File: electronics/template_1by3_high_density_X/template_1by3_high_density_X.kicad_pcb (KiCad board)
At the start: 2 copper layers, 19 x 26.5 mm, 10 parts, among them J1 1, J2 2, J3 3, J4 4, J5 5, J6 6, J7 7, J8 8

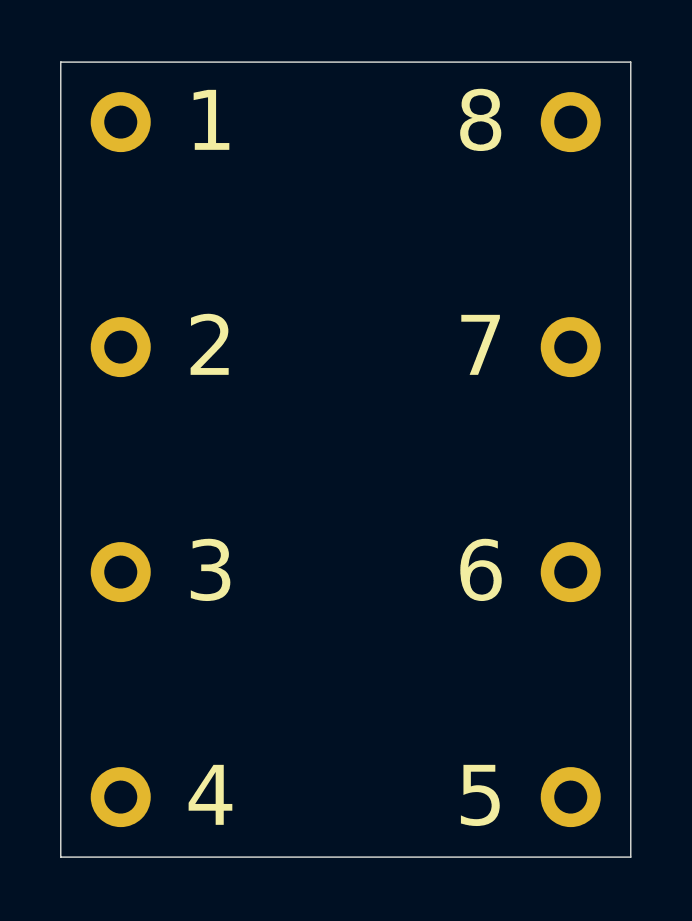
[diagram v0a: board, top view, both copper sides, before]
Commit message: completed high density X templates, updated versionnumbers of high density XN templates
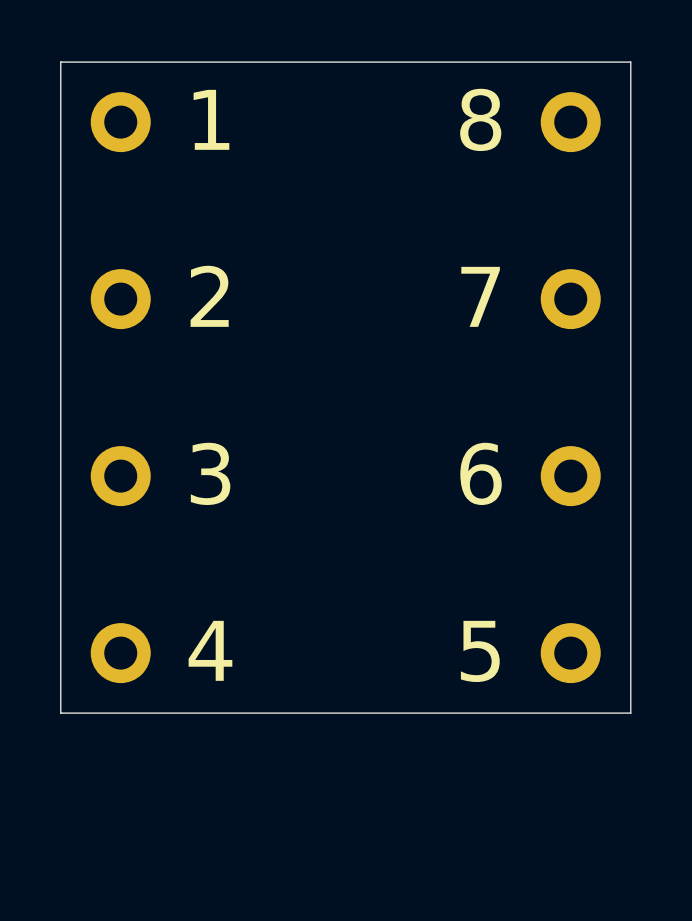
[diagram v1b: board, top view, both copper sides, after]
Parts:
- N1: value V20220113 -> V20240506
- moved J4 4.80 mm to (142.5, 80.2)
- moved J5 4.80 mm to (157.5, 80.2)
- moved J3 3.20 mm to (142.5, 74.3)
- moved J6 3.20 mm to (157.5, 74.3)
- moved N1 2.50 mm to (150.9, 74.7)
- moved N2 2.50 mm to (150.0, 71.0)
- moved J2 1.60 mm to (142.5, 68.4)
- moved J7 1.60 mm to (157.5, 68.4)
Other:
- board size 19 x 26.5 mm -> 19 x 21.7 mm
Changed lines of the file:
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@@
   (footprint "mill-max:PC_pin_nail_head_6092" locked (layer "F.Cu")
     (at 142.5 62.5)
-    (property "Sheetfile" "template_1by3.kicad_sch")
+    (property "Sheetfile" "template_1by3_high_density_X.kicad_sch")
     (property "Sheetname" "")
     (property "ki_description" "Generic connector, single row, 01x01, script generated (kicad-library-utils/schlib/autogen/connector/)")
@@
   )
   (footprint "mill-max:PC_pin_nail_head_6092" locked (layer "F.Cu")
-    (at 142.5 70)
-    (property "Sheetfile" "template_1by3.kicad_sch")
+    (at 142.5 68.4)
+    (property "Sheetfile" "template_1by3_high_density_X.kicad_sch")
     (property "Sheetname" "")
     (property "ki_description" "Generic connector, single row, 01x01, script generated (kicad-library-utils/schlib/autogen/connector/)")
@@
   )
   (footprint "mill-max:PC_pin_nail_head_6092" locked (layer "F.Cu")
-    (at 142.5 77.5)
-    (property "Sheetfile" "template_1by3.kicad_sch")
+    (at 142.5 74.3)
+    (property "Sheetfile" "template_1by3_high_density_X.kicad_sch")
     (property "Sheetname" "")
     (property "ki_description" "Generic connector, single row, 01x01, script generated (kicad-library-utils/schlib/autogen/connector/)")
@@
   )
   (footprint "mill-max:PC_pin_nail_head_6092" locked (layer "F.Cu")
-    (at 157.5 85)
-    (property "Sheetfile" "template_1by3.kicad_sch")
+    (at 157.5 80.2)
+    (property "Sheetfile" "template_1by3_high_density_X.kicad_sch")
     (property "Sheetname" "")
     (property "ki_description" "Generic connector, single row, 01x01, script generated (kicad-library-utils/schlib/autogen/connector/)")
@@
   )
   (footprint "mill-max:PC_pin_nail_head_6092" locked (layer "F.Cu")
-    (at 157.5 77.5)
-    (property "Sheetfile" "template_1by3.kicad_sch")
+    (at 157.5 74.3)
+    (property "Sheetfile" "template_1by3_high_density_X.kicad_sch")
     (property "Sheetname" "")
     (property "ki_description" "Generic connector, single row, 01x01, script generated (kicad-library-utils/schlib/autogen/connector/)")
@@
   )
   (footprint "mill-max:PC_pin_nail_head_6092" locked (layer "F.Cu")
-    (at 142.5 85 180)
-    (property "Sheetfile" "template_1by3.kicad_sch")
+    (at 142.5 80.2 180)
+    (property "Sheetfile" "template_1by3_high_density_X.kicad_sch")
     (property "Sheetname" "")
     (property "ki_description" "Generic connector, single row, 01x01, script generated (kicad-library-utils/schlib/autogen/connector/)")
@@
   (footprint "mill-max:PC_pin_nail_head_6092" locked (layer "F.Cu")
     (at 157.5 62.5)
-    (property "Sheetfile" "template_1by3.kicad_sch")
+    (property "Sheetfile" "template_1by3_high_density_X.kicad_sch")
     (property "Sheetname" "")
     (property "ki_description" "Generic connector, single row, 01x01, script generated (kicad-library-utils/schlib/autogen/connector/)")
@@
   )
   (footprint "mill-max:PC_pin_nail_head_6092" locked (layer "F.Cu")
-    (at 157.5 70)
-    (property "Sheetfile" "template_1by3.kicad_sch")
+    (at 157.5 68.4)
+    (property "Sheetfile" "template_1by3_high_density_X.kicad_sch")
     (property "Sheetname" "")
     (property "ki_description" "Generic connector, single row, 01x01, script generated (kicad-library-utils/schlib/autogen/connector/)")
@@
   )
   (footprint "Symbol:OSHW-Symbol_6.7x6mm_SilkScreen" (layer "B.Cu")
-    (at 150 73.5 180)
+    (at 150 71 180)
     (descr "Open Source Hardware Symbol")
     (tags "Logo Symbol OSHW")
-    (property "Sheetfile" "template_1by3.kicad_sch")
+    (property "Sheetfile" "template_1by3_high_density_X.kicad_sch")
     (property "Sheetname" "")
     (attr exclude_from_pos_files)
@@
   )
   (footprint "SquantorLabels:Label_Generic" (layer "B.Cu")
-    (at 150.9 77.2 180)
+    (at 150.9 74.7 180)
     (descr "Label for general purpose use")
     (tags "Label")
-    (property "Sheetfile" "template_1by3.kicad_sch")
+    (property "Sheetfile" "template_1by3_high_density_X.kicad_sch")
     (property "Sheetname" "")
     (attr smd)
@@
         (effects (font (size 1 1) (thickness 0.15)) (justify mirror))
     )
-    (fp_text value "V20220113" (at 0.8 0.1) (layer "B.SilkS")
+    (fp_text value "V20240506" (at 0.8 0.1) (layer "B.SilkS")
         (effects (font (size 0.8 0.8) (thickness 0.15)) (justify mirror))
     )
@@
       (stroke (width 0.15) (type solid)) (layer "B.SilkS"))
   )
-  (gr_line (start 140.5 87) (end 159.5 87)
+  (gr_line (start 140.5 82.2) (end 159.5 82.2)
     (stroke (width 0.05) (type solid)) (layer "Edge.Cuts"))
-  (gr_line (start 159.5 60.5) (end 159.5 87)
+  (gr_line (start 159.5 60.5) (end 159.5 82.2)
     (stroke (width 0.05) (type solid)) (layer "Edge.Cuts"))
   (gr_line (start 159.5 60.5) (end 140.5 60.5)
     (stroke (width 0.05) (type solid)) (layer "Edge.Cuts"))
-  (gr_line (start 140.5 87) (end 140.5 60.5)
+  (gr_line (start 140.5 82.2) (end 140.5 60.5)
     (stroke (width 0.05) (type solid)) (layer "Edge.Cuts"))
 )
